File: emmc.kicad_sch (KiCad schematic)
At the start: 27 parts, among them U3 EMMC32G-TS0A-01011

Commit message: [#83609] Reannotate board
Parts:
- renumbered C80 to C22, C86 to C23, C81 to C24, C112 to C25, C82 to C26, C119 to C27, C83 to C28, C120 to C29, C84 to C30, C121 to C31, C85 to C32, C122 to C33, C123 to C34, C118 to C35, R1 to R100, R2 to R101, R3 to R102, R4 to R103, R5 to R104, R6 to R105, R7 to R106, R8 to R107, R9 to R108, R10 to R109, R289 to R98, R288 to R99, U3 to U6

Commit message: [#83736] WIP: Clear ERC
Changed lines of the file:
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@@
 	)
 	(junction
+		(at 185.42 119.38)
+		(diameter 0)
+		(color 0 0 0 0)
+	)
+	(junction
 		(at 236.22 132.08)
 		(diameter 0)
@@
 	)
 	(junction
+		(at 177.8 102.87)
+		(diameter 0)
+		(color 0 0 0 0)
+	)
+	(junction
 		(at 121.92 102.87)
 		(diameter 0)
@@
 	(wire
 		(pts
+			(xy 185.42 119.38) (xy 195.58 119.38)
+		)
+		(stroke
+			(width 0)
+			(type default)
+		)
+	)
+	(wire
+		(pts
 			(xy 224.79 110.49) (xy 224.79 137.16)
 		)
@@
 	(wire
 		(pts
+			(xy 177.8 101.6) (xy 177.8 102.87)
+		)
+		(stroke
+			(width 0)
+			(type default)
+		)
+	)
+	(wire
+		(pts
 			(xy 260.35 147.32) (xy 260.35 149.86)
 		)
@@
 	(wire
 		(pts
-			(xy 177.8 119.38) (xy 195.58 119.38)
+			(xy 177.8 119.38) (xy 185.42 119.38)
 		)
 		(stroke
@@
 	(wire
 		(pts
+			(xy 185.42 115.57) (xy 185.42 119.38)
+		)
+		(stroke
+			(width 0)
+			(type default)
+		)
+	)
+	(wire
+		(pts
 			(xy 151.13 128.27) (xy 151.13 127)
 		)
@@
 	)
 	(symbol
+		(lib_id "antmicropower:PWR_FLAG")
+		(at 177.8 101.6 0)
+		(unit 1)
+		(exclude_from_sim no)
+		(in_bom yes)
+		(on_board yes)
+		(dnp no)
+		(property "Reference" "#FLG011"
+			(at 177.8 99.695 0)
+			(effects
+				(font
+					(size 1.27 1.27)
+				)
+				(hide yes)
+			)
+		)
+		(property "Value" "PWR_FLAG"
+			(at 177.8 97.79 0)
+			(effects
+				(font
+					(size 1.27 1.27)
+				)
+			)
+		)
+		(property "Footprint" ""
+			(at 177.8 101.6 0)
+			(effects
+				(font
+					(size 1.27 1.27)
+				)
+				(hide yes)
+			)
+		)
+		(property "Datasheet" ""
+			(at 177.8 101.6 0)
+			(effects
+				(font
+					(size 1.27 1.27)
+				)
+				(hide yes)
+			)
+		)
+		(property "Description" ""
+			(at 177.8 101.6 0)
+			(effects
+				(font
+					(size 1.27 1.27)
+				)
+				(hide yes)
+			)
+		)
+		(pin "1"
+		)
+		(instances
+			(project ""
+				(path "/5f636c45-3c15-4731-8931-4625e0dab7e4/af9b114c-dfa4-427f-a7c0-6a1753518223"
+					(reference "#FLG011")
+					(unit 1)
+				)
+			)
+		)
+	)
+	(symbol
 		(lib_id "antmicropower:GND")
 		(at 151.13 128.27 0)
@@
 					(unit 1)
 				)
+			)
+		)
+	)
+	(symbol
+		(lib_id "antmicropower:PWR_FLAG")
+		(at 185.42 115.57 0)
+		(unit 1)
+		(exclude_from_sim no)
+		(in_bom yes)
+		(on_board yes)
+		(dnp no)
+		(property "Reference" "#FLG018"
+			(at 185.42 113.665 0)
+			(effects
+				(font
+					(size 1.27 1.27)
+				)
+				(hide yes)
+			)
+		)
+		(property "Value" "PWR_FLAG"
+			(at 185.42 111.76 0)
+			(effects
+				(font
+					(size 1.27 1.27)
+				)
+			)
+		)
+		(property "Footprint" ""
+			(at 185.42 115.57 0)
+			(effects
+				(font
+					(size 1.27 1.27)
+				)
+				(hide yes)
+			)
+		)
+		(property "Datasheet" ""
+			(at 185.42 115.57 0)
+			(effects
+				(font
+					(size 1.27 1.27)
+				)
+				(hide yes)
+			)
+		)
+		(property "Description" ""
+			(at 185.42 115.57 0)
+			(effects
+				(font
+					(size 1.27 1.27)
+				)
+				(hide yes)
+			)
+		)
+		(pin "1"
+		)
+		(instances
+			(project "bmc-reference-carrier-board"
+				(path "/5f636c45-3c15-4731-8931-4625e0dab7e4/af9b114c-dfa4-427f-a7c0-6a1753518223"
+					(reference "#FLG018")
+					(unit 1)
+				)

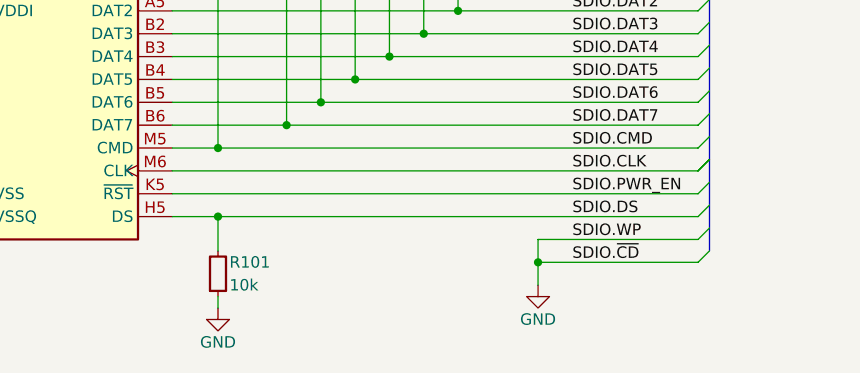
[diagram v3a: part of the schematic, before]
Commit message: [#83767] Fix SDIO net class assignment, synchronize PCB with schematic
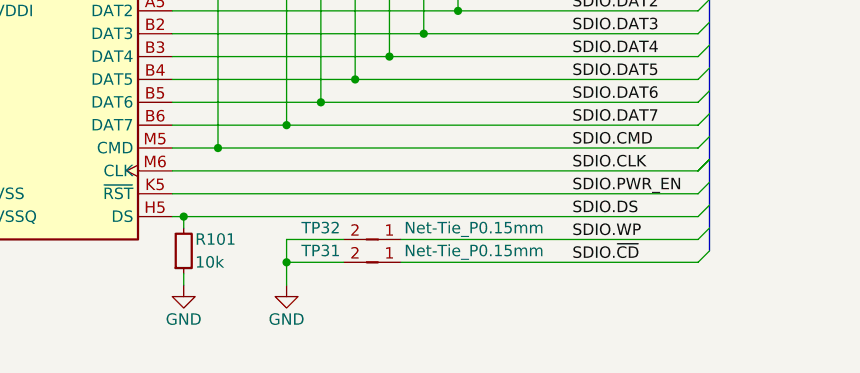
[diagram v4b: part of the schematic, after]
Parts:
- added TP31, TP32: Net-Tie_P0.15mm, antmicro-footprints:NetTie-2_SMD_Pad0.15mm, symbol antmicroShuntsJumpers:Net-Tie_P0.15mm
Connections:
- net GND: now also TP31.2, TP32.2
- new net SDIO.WP: TP32.1
- new net SDIO.~{CD}: TP31.1
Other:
- moved on the sheet: R101

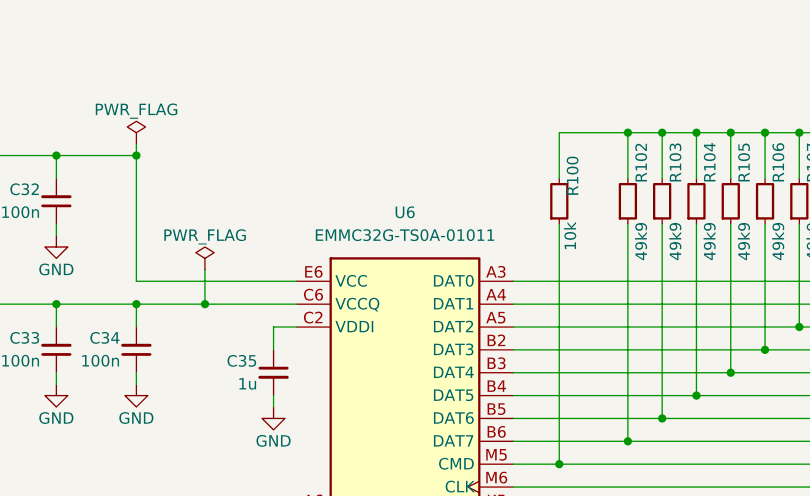
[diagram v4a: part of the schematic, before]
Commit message: [#83767] Update eMMC from lib
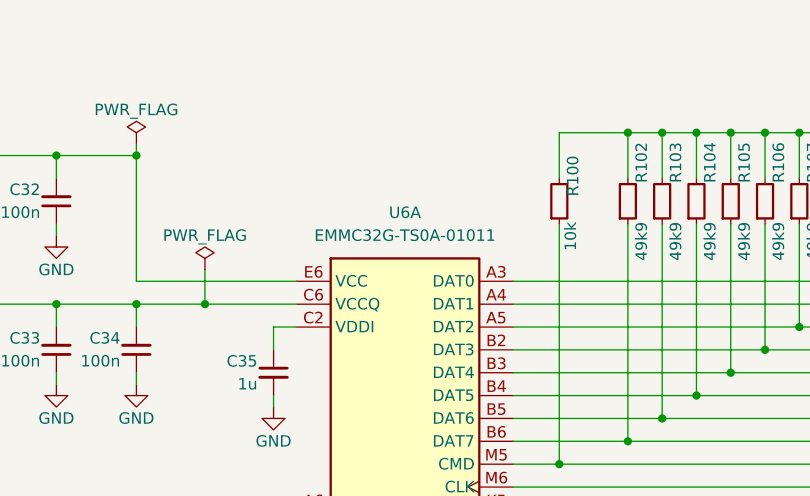
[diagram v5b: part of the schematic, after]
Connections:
- now unconnected: U6.A7 (RFU), U6.E10 (VSF), U6.E5 (RFU), U6.E8 (RFU), U6.E9 (VSF), U6.F10 (VSF), U6.G10 (RFU), U6.G3 (RFU), U6.K10 (RFU), U6.K6 (RFU), U6.K7 (RFU), U6.P10 (RFU), U6.P7 (RFU)

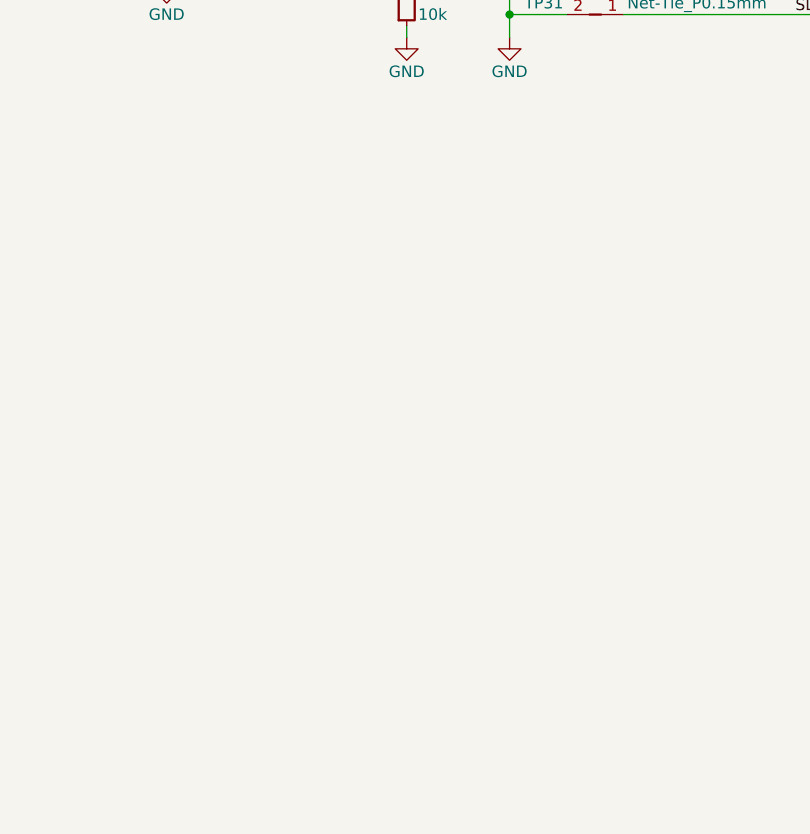
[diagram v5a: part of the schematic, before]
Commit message: [#83767] Sync PCB from schematic
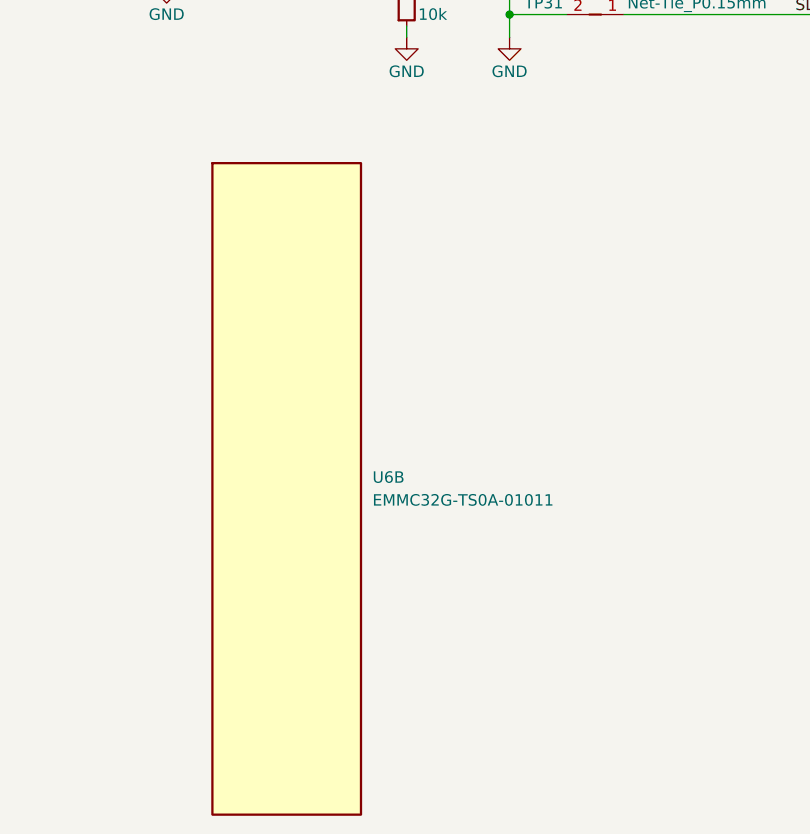
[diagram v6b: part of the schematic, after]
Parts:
- added unit 2 of U6

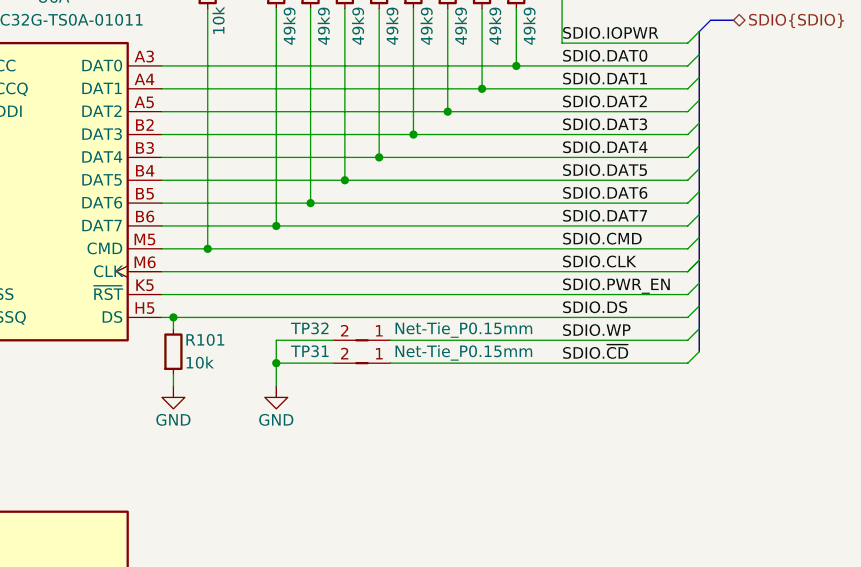
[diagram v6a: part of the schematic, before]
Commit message: [#83767] Add more I2C connections
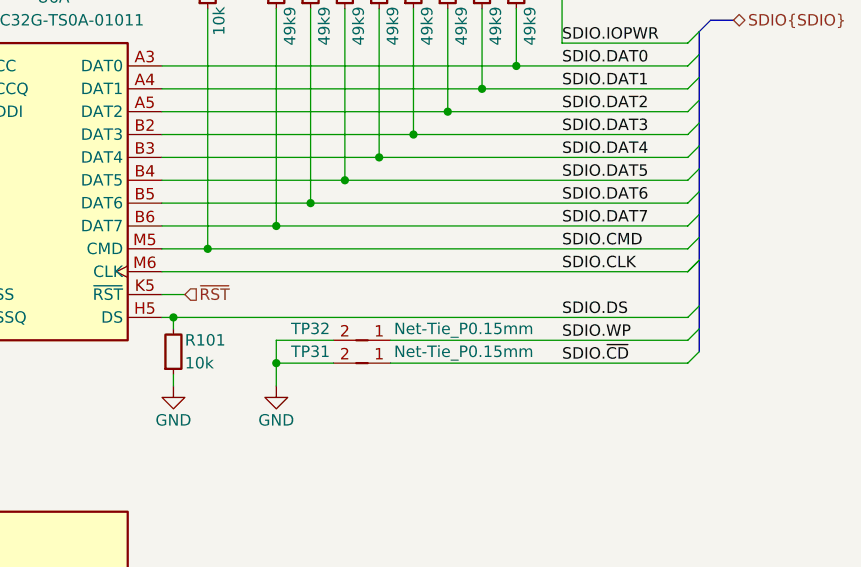
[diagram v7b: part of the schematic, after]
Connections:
- net SDIO.PWR_EN renamed ~{RST}
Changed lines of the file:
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@@
-	)
-	(bus_entry
-		(at 279.4 140.97)
-		(size -1.27 1.27)
-		(stroke
-			(width 0)
-			(type default)
-		)
 	)
 	(bus_entry
@@
 		)
 	)
-	(bus
-		(pts
-			(xy 279.4 138.43) (xy 279.4 140.97)
-		)
-		(stroke
-			(width 0)
-			(type default)
-		)
-	)
 	(wire
 		(pts
@@
 	(bus
 		(pts
-			(xy 279.4 140.97) (xy 279.4 143.51)
+			(xy 279.4 138.43) (xy 279.4 143.51)
 		)
 		(stroke
@@
 		)
 	)
+	(wire
+		(pts
+			(xy 222.25 142.24) (xy 219.71 142.24)
+		)
+		(stroke
+			(width 0)
+			(type default)
+		)
+	)
 	(bus
 		(pts
@@
 		(pts
 			(xy 121.92 119.38) (xy 130.81 119.38)
-		)
-		(stroke
-			(width 0)
-			(type default)
-		)
-	)
-	(wire
-		(pts
-			(xy 219.71 142.24) (xy 278.13 142.24)
 		)
 		(stroke
@@
 	(label "SDIO.IOPWR"
 		(at 264.16 114.3 0)
-		(effects
-			(font
-				(size 1.27 1.27)
-			)
-			(justify left bottom)
-		)
-	)
-	(label "SDIO.PWR_EN"
-		(at 264.16 142.24 0)
 		(effects
 			(font
@@
 		(effects
 			(font
+				(size 1.27 1.27)
+			)
+			(justify left)
+		)
+	)
+	(hierarchical_label "~{RST}"
+		(shape input)
+		(at 222.25 142.24 0)
+		(effects
+			(font
